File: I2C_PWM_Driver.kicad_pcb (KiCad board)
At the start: 2 copper layers, 89 x 42 mm, 97 parts, among them J1 Screw_Terminal_01x02, J2 Conn_01x02_Male, J3 Screw_Terminal_01x02, J4 Conn_02x08_Odd_Even, Q1 DMG2305UX, Q10 DMG2305UX, Q11 BC817, Q12 BC817, Q13 DMG2305UX, Q14 DMG2305UX, Q15 BC817, Q16 BC817, Q17 DMG2305UX, Q18 DMG2305UX, Q19 BC817, Q2 DMG2305UX, Q20 BC817, Q21 DMG2305UX, Q22 DMG2305UX, Q23 BC817, Q24 BC817, Q25 DMG2305UX, Q26 DMG2305UX, Q27 BC817, Q28 BC817, Q29 DMG2305UX, Q3 BC817, Q30 DMG2305UX, Q31 BC817, Q32 BC817, Q4 BC817, Q5 DMG2305UX, Q6 DMG2305UX, Q7 BC817, Q8 BC817, Q9 DMG2305UX, SW1 SW_Push, U1 PCA9685PW, U2 LM2931-5.0_SO8

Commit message: Updated resistor valuesUpdated resistor valuesUpdated resistor valuesUpdated resistor values
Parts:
- R1, R10, R11, R16, R17, R2, R20, R21, R25, R26, R36, R37, R41, R42, R5, R6: value R -> 1k
- R14, R15, R18, R19, R22, R23, R3, R33, R34, R39, R4, R40, R43, R44, R7, R8: value R -> 10k
- R38: value 68k -> 39k

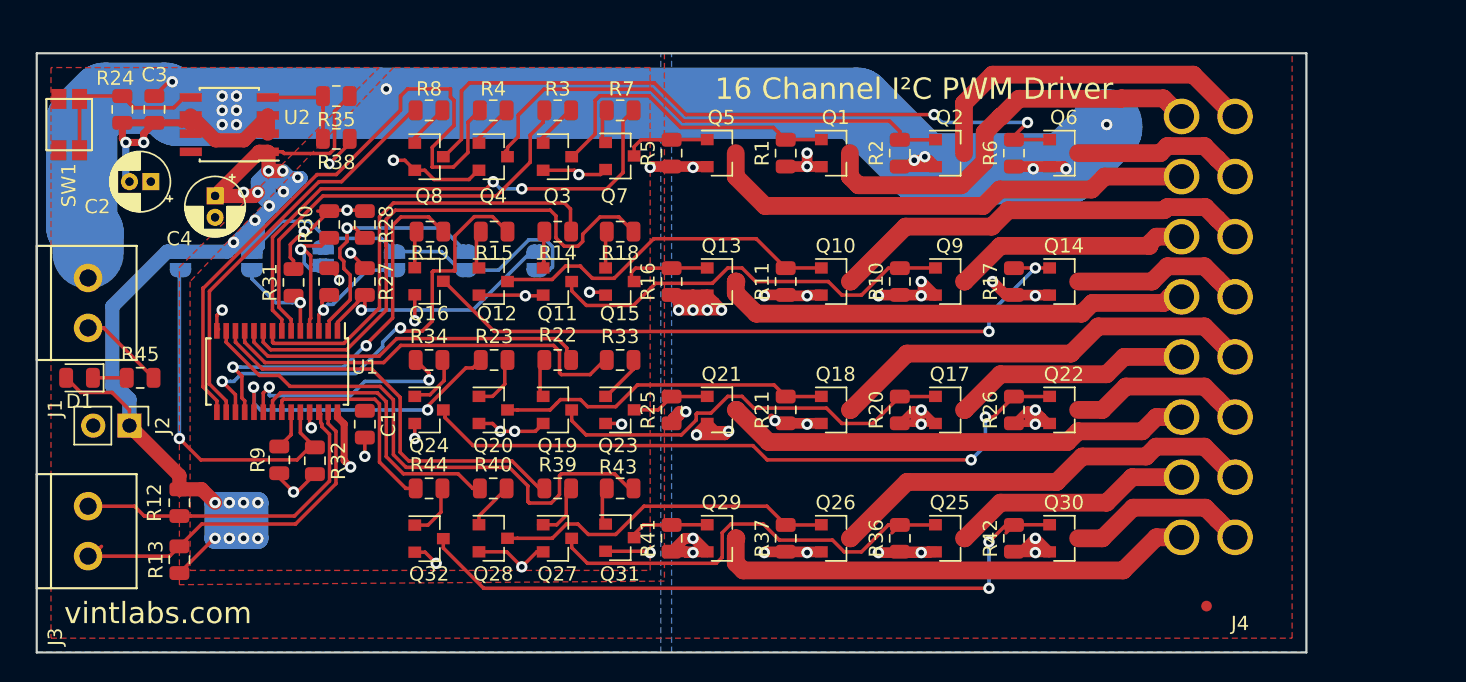
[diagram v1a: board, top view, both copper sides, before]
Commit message: Removed SW1 (reset - never used)
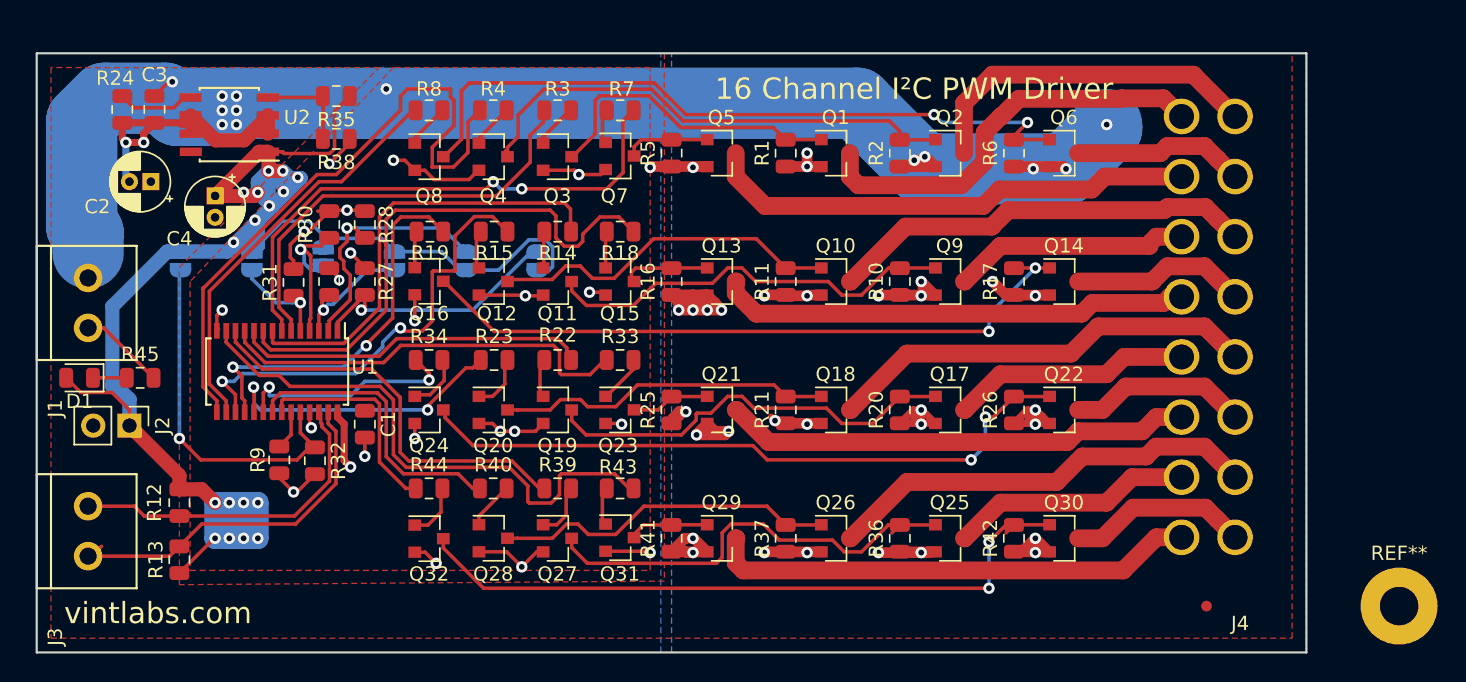
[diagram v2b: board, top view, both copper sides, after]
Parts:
- removed SW1: SW_Push, reset:EVQ Tactile Switch
- added REF**: MountingHole_2.7mm_Pad, MountingHole:MountingHole_2.7mm_Pad, F.Cu at (169.5, 86.8)
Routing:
- net Net-(R24-Pad1): track 12.1 -> 5.43 mm
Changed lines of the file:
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@@
     (thickness 1.6)
     (drawings 21)
-    (tracks 1026)
+    (tracks 1023)
     (zones 0)
     (modules 97)
@@
     (add_net VCC)
   )
+  (module MountingHole:MountingHole_2.7mm_Pad (layer F.Cu)
+    (at 169.5 86.75)
+    (descr "Mounting Hole 2.7mm")
+    (tags "mounting hole 2.7mm")
+    (attr virtual)
+    (fp_text reference REF** (at 0 -3.7) (layer F.SilkS)
+      (effects (font (size 1 1) (thickness 0.15)))
+    )
+    (fp_text value MountingHole_2.7mm_Pad (at 0 3.7) (layer F.Fab)
+      (effects (font (size 1 1) (thickness 0.15)))
+    )
+    (fp_circle (center 0 0) (end 2.95 0) (layer F.CrtYd) (width 0.05))
+    (fp_circle (center 0 0) (end 2.7 0) (layer Cmts.User) (width 0.15))
+    (fp_text user %R (at 0.3 0) (layer F.Fab)
+      (effects (font (size 1 1) (thickness 0.15)))
+    )
+    (pad 1 thru_hole circle (at 0 0) (size 5.4 5.4) (drill 2.7) (layers *.Cu *.Mask))
+  )
   (module LED_SMD:LED_0805_2012Metric (layer F.Cu)
     (at 77 70.75 180)
@@
       (net 34 SCL))
   )
-  (module "reset:EVQ Tactile Switch" (layer F.Cu)
-    (at 76.275 53 270)
-    (fp_text reference SW1 (at 4.25 0.025 270) (layer F.SilkS)
-      (effects (font (size 1 1) (thickness 0.15)))
-    )
-    (fp_text value SW_Push (at 0.5 3.3 270) (layer F.Fab)
-      (effects (font (size 1 1) (thickness 0.15)))
-    )
-    (fp_line (start -2.7 2.7) (end -2.7 -1.9) (layer F.CrtYd) (width 0.15))
-    (fp_line (start 2.8 2.7) (end -2.7 2.7) (layer F.CrtYd) (width 0.15))
-    (fp_line (start 2.8 -1.9) (end 2.8 2.7) (layer F.CrtYd) (width 0.15))
-    (fp_line (start -2.7 -1.9) (end 2.8 -1.9) (layer F.CrtYd) (width 0.15))
-    (fp_line (start -0.8 2.1) (end -0.7 1.6) (layer Dwgs.User) (width 0.15))
-    (fp_line (start 0.8 2.1) (end 0.7 1.6) (layer Dwgs.User) (width 0.15))
-    (fp_line (start 0.85 2.1) (end -0.85 2.1) (layer Dwgs.User) (width 0.15))
-    (fp_line (start 1.8 1.6) (end 1.8 -1.6) (layer F.SilkS) (width 0.15))
-    (fp_line (start -1.8 -1.6) (end -1.8 1.6) (layer F.SilkS) (width 0.15))
-    (fp_line (start -1.75 1.6) (end 1.75 1.6) (layer F.SilkS) (width 0.15))
-    (fp_line (start -1.75 -1.6) (end 1.75 -1.6) (layer F.SilkS) (width 0.15))
-    (pad 2 smd rect (at 1.8 0.725 270) (size 1.4 1.05) (layers F.Cu F.Paste F.Mask)
-      (net 4 +VDC))
-    (pad 2 smd rect (at -1.8 0.725 270) (size 1.4 1.05) (layers F.Cu F.Paste F.Mask)
-      (net 4 +VDC))
-    (pad 1 smd rect (at 1.8 -0.725 270) (size 1.4 1.05) (layers F.Cu F.Paste F.Mask)
-      (net 78 "Net-(R24-Pad1)"))
-    (pad 1 smd rect (at -1.8 -0.725 270) (size 1.4 1.05) (layers F.Cu F.Paste F.Mask)
-      (net 78 "Net-(R24-Pad1)"))
-  )
   (module Connector_PinHeader_2.54mm:PinHeader_1x02_P2.54mm_Vertical (layer F.Cu)
     (at 80.5 74.1 270)
@@
   (segment (start 84.325 51.095) (end 83.60749 51.81251) (width 0.25) (layer F.Cu) (net 78))
   (segment (start 84.8 51.095) (end 84.325 51.095) (width 0.25) (layer F.Cu) (net 78))
-  (segment (start 77.2 51) (end 77 51.2) (width 0.25) (layer F.Cu) (net 78))
-  (segment (start 80 51) (end 77.2 51) (width 0.25) (layer F.Cu) (net 78))
-  (segment (start 77 51.2) (end 77 54.8) (width 0.25) (layer F.Cu) (net 78))
   (segment (start 77.9375 70.75) (end 80.3125 70.75) (width 0.25) (layer F.Cu) (net 79))
   (zone (net 4) (net_name +VDC) (layer F.Cu) (hatch edge 0.508)

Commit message: Routing complete (pending audit)
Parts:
- added JP7: SolderJumper_3_Bridged12, Jumper:SolderJumper-3_P1.3mm_Bridged12_RoundedPad1.0x1.5mm, B.Cu at (96.0, 55.8)
- added R46: 69k, Resistor_SMD:R_0805_2012Metric, F.Cu at (97.0, 55.8)
- added REF**: MountingHole_2.7mm_Pad, MountingHole:MountingHole_2.7mm_Pad, F.Cu at (160.0, 51.0)
- added REF**: MountingHole_2.7mm_Pad, MountingHole:MountingHole_2.7mm_Pad, F.Cu at (77.0, 87.0)
- C2: footprint Capacitor_THT:CP_Radial_D4.0mm_P1.50mm -> Capacitor_SMD:C_0805_2012Metric_Pad1.15x1.40mm_HandSolder
- C4: value 100u -> 47u; footprint Capacitor_THT:CP_Radial_D4.0mm_P1.50mm -> Capacitor_SMD:CP_Elec_6.3x5.9
- J3: footprint PWM_Conn:SCREW TERMINAL BLOCK 3.5MM 2POS -> Connector_PinHeader_2.54mm:PinHeader_1x02_P2.54mm_Vertical
- moved REF** 9.50 mm to (160.0, 87.0)
- moved REF** 9.09 mm to (147.0, 88.0)
- moved R24 5.26 mm to (77.5, 56.6)
- moved J3 4.78 mm to (77.8, 78.6), turned to 0 degrees
- moved J4 3.62 mm to (148.5, 85.9)
- moved C4 2.96 mm to (86.2, 61.0)
- moved C3 2.12 mm to (82.2, 54.1)
- moved C2 2.07 mm to (80.0, 56.5), turned to 270 degrees
- moved R38 1.88 mm to (94.5, 55.8), turned to 90 degrees
- moved R35 0.95 mm to (94.5, 51.8), turned to 90 degrees
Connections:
- R35 pad 2: Net-(R35-Pad2) -> Net-(JP7-Pad2)
- R38 pad 2: Net-(R35-Pad2) -> Net-(JP7-Pad1)
- U2 pad 4: Net-(R35-Pad2) -> Net-(JP7-Pad2)
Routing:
- net GND: track 86.9 -> 123.2 mm, vias 23 -> 31
- net Net-(JP7-Pad2): track 0.00 -> 15.2 mm, vias 0 -> 1
- net VCC: track 133.2 -> 141.3 mm, vias 18 -> 16
- net Sig9: track 28.5 -> 36.6 mm
- net Net-(R35-Pad2): track 6.90 -> 0.00 mm
- net Net-(JP7-Pad1): track 0.00 -> 5.89 mm, vias 0 -> 1
- net Out1: track 34.6 -> 29.4 mm
- net Out0: track 29.4 -> 24.6 mm
- net Out7: track 34.2 -> 30.0 mm
- net Net-(JP7-Pad3): track 0.00 -> 4.08 mm, vias 0 -> 1
- net Out11: track 12.3 -> 8.25 mm
- net Out12: track 30.3 -> 26.3 mm
- net Out14: track 30.5 -> 26.5 mm
- net Out13: track 12.6 -> 8.52 mm
- net Out15: track 12.7 -> 8.76 mm
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- removed copper zone on F.Cu, net VCC
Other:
- board text added: "+"
